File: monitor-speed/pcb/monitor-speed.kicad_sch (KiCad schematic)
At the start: 1 part

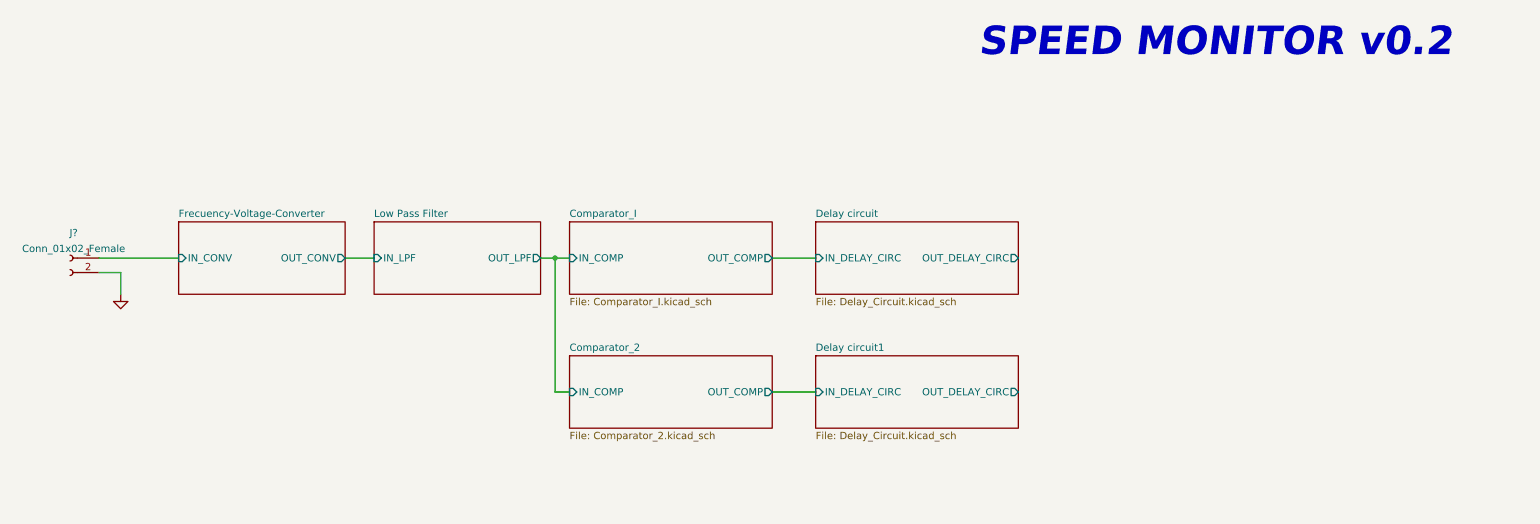
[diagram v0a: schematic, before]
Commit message: Monitor-Speed: Add pcb edge
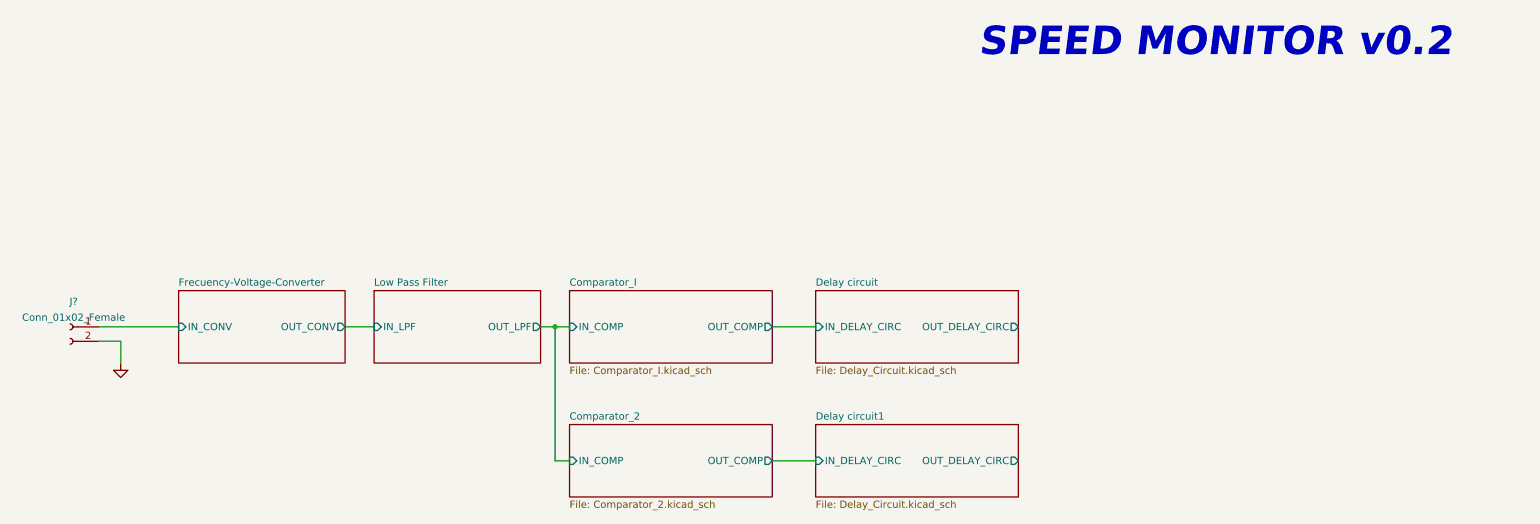
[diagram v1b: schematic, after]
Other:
- moved on the sheet: J?
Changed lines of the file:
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@@
 (kicad_sch (version 20211123) (generator eeschema)
   (paper "A4")
-  (junction (at 114.935 65.405) (diameter 0) (color 0 0 0 0)
+  (junction (at 114.935 77.47) (diameter 0) (color 0 0 0 0)
   )
-  (wire (pts (xy 78.105 65.405) (xy 83.185 65.405))
+  (wire (pts (xy 78.105 77.47) (xy 83.185 77.47))
     (stroke (width 0) (type default) (color 0 0 0 0))
   )
-  (wire (pts (xy 114.935 65.405) (xy 117.475 65.405))
+  (wire (pts (xy 114.935 77.47) (xy 117.475 77.47))
     (stroke (width 0) (type default) (color 0 0 0 0))
   )
-  (wire (pts (xy 153.035 88.9) (xy 160.655 88.9))
+  (wire (pts (xy 153.035 100.965) (xy 160.655 100.965))
     (stroke (width 0) (type default) (color 0 0 0 0))
   )
-  (wire (pts (xy 34.925 65.405) (xy 48.895 65.405))
+  (wire (pts (xy 34.925 77.47) (xy 48.895 77.47))
     (stroke (width 0) (type default) (color 0 0 0 0))
   )
-  (wire (pts (xy 38.735 67.945) (xy 38.735 71.755))
+  (wire (pts (xy 38.735 80.01) (xy 38.735 83.82))
     (stroke (width 0) (type default) (color 0 0 0 0))
   )
-  (wire (pts (xy 114.935 65.405) (xy 114.935 88.9))
+  (wire (pts (xy 114.935 77.47) (xy 114.935 100.965))
     (stroke (width 0) (type default) (color 0 0 0 0))
   )
-  (wire (pts (xy 153.035 65.405) (xy 160.655 65.405))
+  (wire (pts (xy 153.035 77.47) (xy 160.655 77.47))
     (stroke (width 0) (type default) (color 0 0 0 0))
   )
-  (wire (pts (xy 114.935 88.9) (xy 117.475 88.9))
+  (wire (pts (xy 114.935 100.965) (xy 117.475 100.965))
     (stroke (width 0) (type default) (color 0 0 0 0))
   )
-  (wire (pts (xy 34.925 67.945) (xy 38.735 67.945))
+  (wire (pts (xy 34.925 80.01) (xy 38.735 80.01))
     (stroke (width 0) (type default) (color 0 0 0 0))
   )
-  (wire (pts (xy 112.395 65.405) (xy 114.935 65.405))
+  (wire (pts (xy 112.395 77.47) (xy 114.935 77.47))
     (stroke (width 0) (type default) (color 0 0 0 0))
   )
@@
     (effects (font (size 5 5) (thickness 1) bold italic) (justify left bottom))
   )
-  (symbol (lib_id "power:GND") (at 38.735 71.755 0) (unit 1)
+  (symbol (lib_id "power:GND") (at 38.735 83.82 0) (unit 1)
     (in_bom yes) (on_board yes) (fields_autoplaced)
-    (property "Reference" "#PWR?" (id 0) (at 38.735 78.105 0)
+    (property "Reference" "#PWR?" (id 0) (at 38.735 90.17 0)
       (effects (font (size 1.27 1.27)) hide)
     )
-    (property "Value" "GND" (id 1) (at 38.735 76.3175 0)
+    (property "Value" "GND" (id 1) (at 38.735 88.3825 0)
       (effects (font (size 1.27 1.27)) hide)
     )
-    (property "Footprint" "" (id 2) (at 38.735 71.755 0)
+    (property "Footprint" "" (id 2) (at 38.735 83.82 0)
       (effects (font (size 1.27 1.27)) hide)
     )
-    (property "Datasheet" "" (id 3) (at 38.735 71.755 0)
+    (property "Datasheet" "" (id 3) (at 38.735 83.82 0)
       (effects (font (size 1.27 1.27)) hide)
     )
     (pin "1")
   )
-  (symbol (lib_id "Connector:Conn_01x02_Female") (at 29.845 65.405 0) (mirror y) (unit 1)
+  (symbol (lib_id "Connector:Conn_01x02_Female") (at 29.845 77.47 0) (mirror y) (unit 1)
     (in_bom yes) (on_board yes) (fields_autoplaced)
-    (property "Reference" "J?" (id 0) (at 30.48 60.9813 0))
-    (property "Value" "Conn_01x02_Female" (id 1) (at 30.48 63.7564 0))
-    (property "Footprint" "" (id 2) (at 29.845 65.405 0)
+    (property "Reference" "J?" (id 0) (at 30.48 73.0463 0))
+    (property "Value" "Conn_01x02_Female" (id 1) (at 30.48 75.8214 0))
+    (property "Footprint" "" (id 2) (at 29.845 77.47 0)
       (effects (font (size 1.27 1.27)) hide)
     )
-    (property "Datasheet" "~" (id 3) (at 29.845 65.405 0)
+    (property "Datasheet" "~" (id 3) (at 29.845 77.47 0)
       (effects (font (size 1.27 1.27)) hide)
     )
@@
     (pin "2")
   )
-  (sheet (at 48.895 59.055) (size 29.21 12.7) (fields_autoplaced)
+  (sheet (at 48.895 71.12) (size 29.21 12.7) (fields_autoplaced)
     (stroke (width 0.1524) (type solid) (color 0 0 0 0))
     (fill (color 0 0 0 0.0000))
-    (property "Sheet name" "Frecuency-Voltage-Converter" (id 0) (at 48.895 58.3434 0)
+    (property "Sheet name" "Frecuency-Voltage-Converter" (id 0) (at 48.895 70.4084 0)
       (effects (font (size 1.27 1.27)) (justify left bottom))
     )
-    (property "Sheet file" "Frecuency_voltage_converter.kicad_sch" (id 1) (at 48.895 72.3396 0)
+    (property "Sheet file" "Frecuency_voltage_converter.kicad_sch" (id 1) (at 48.895 84.4046 0)
       (effects (font (size 1.27 1.27)) (justify left top) hide)
     )
-    (pin "IN_CONV" input (at 48.895 65.405 180)
+    (pin "IN_CONV" input (at 48.895 77.47 180)
       (effects (font (size 1.27 1.27)) (justify left))
     )
-    (pin "OUT_CONV" output (at 78.105 65.405 0)
+    (pin "OUT_CONV" output (at 78.105 77.47 0)
       (effects (font (size 1.27 1.27)) (justify right))
     )
   )
-  (sheet (at 160.655 82.55) (size 35.56 12.7) (fields_autoplaced)
+  (sheet (at 160.655 94.615) (size 35.56 12.7) (fields_autoplaced)
     (stroke (width 0.1524) (type solid) (color 0 0 0 0))
     (fill (color 0 0 0 0.0000))
-    (property "Sheet name" "Delay circuit1" (id 0) (at 160.655 81.8384 0)
+    (property "Sheet name" "Delay circuit1" (id 0) (at 160.655 93.9034 0)
       (effects (font (size 1.27 1.27)) (justify left bottom))
     )
-    (property "Sheet file" "Delay_Circuit.kicad_sch" (id 1) (at 160.655 95.8346 0)
+    (property "Sheet file" "Delay_Circuit.kicad_sch" (id 1) (at 160.655 107.8996 0)
       (effects (font (size 1.27 1.27)) (justify left top))
     )
-    (pin "IN_DELAY_CIRC" input (at 160.655 88.9 180)
+    (pin "IN_DELAY_CIRC" input (at 160.655 100.965 180)
       (effects (font (size 1.27 1.27)) (justify left))
     )
-    (pin "OUT_DELAY_CIRC" output (at 196.215 88.9 0)
+    (pin "OUT_DELAY_CIRC" output (at 196.215 100.965 0)
       (effects (font (size 1.27 1.27)) (justify right))
     )
   )
-  (sheet (at 117.475 82.55) (size 35.56 12.7) (fields_autoplaced)
+  (sheet (at 117.475 94.615) (size 35.56 12.7) (fields_autoplaced)
     (stroke (width 0.1524) (type solid) (color 0 0 0 0))
     (fill (color 0 0 0 0.0000))
-    (property "Sheet name" "Comparator_2" (id 0) (at 117.475 81.8384 0)
+    (property "Sheet name" "Comparator_2" (id 0) (at 117.475 93.9034 0)
       (effects (font (size 1.27 1.27)) (justify left bottom))
     )
-    (property "Sheet file" "Comparator_2.kicad_sch" (id 1) (at 117.475 95.8346 0)
+    (property "Sheet file" "Comparator_2.kicad_sch" (id 1) (at 117.475 107.8996 0)
       (effects (font (size 1.27 1.27)) (justify left top))
     )
-    (pin "IN_COMP" input (at 117.475 88.9 180)
+    (pin "IN_COMP" input (at 117.475 100.965 180)
       (effects (font (size 1.27 1.27)) (justify left))
     )
-    (pin "OUT_COMP" output (at 153.035 88.9 0)
+    (pin "OUT_COMP" output (at 153.035 100.965 0)
       (effects (font (size 1.27 1.27)) (justify right))
     )
   )
-  (sheet (at 160.655 59.055) (size 35.56 12.7) (fields_autoplaced)
+  (sheet (at 160.655 71.12) (size 35.56 12.7) (fields_autoplaced)
     (stroke (width 0.1524) (type solid) (color 0 0 0 0))
     (fill (color 0 0 0 0.0000))
-    (property "Sheet name" "Delay circuit" (id 0) (at 160.655 58.3434 0)
+    (property "Sheet name" "Delay circuit" (id 0) (at 160.655 70.4084 0)
       (effects (font (size 1.27 1.27)) (justify left bottom))
     )
-    (property "Sheet file" "Delay_Circuit.kicad_sch" (id 1) (at 160.655 72.3396 0)
+    (property "Sheet file" "Delay_Circuit.kicad_sch" (id 1) (at 160.655 84.4046 0)
       (effects (font (size 1.27 1.27)) (justify left top))
     )
-    (pin "IN_DELAY_CIRC" input (at 160.655 65.405 180)
+    (pin "IN_DELAY_CIRC" input (at 160.655 77.47 180)
       (effects (font (size 1.27 1.27)) (justify left))
     )
-    (pin "OUT_DELAY_CIRC" output (at 196.215 65.405 0)
+    (pin "OUT_DELAY_CIRC" output (at 196.215 77.47 0)
       (effects (font (size 1.27 1.27)) (justify right))
     )
   )
-  (sheet (at 117.475 59.055) (size 35.56 12.7) (fields_autoplaced)
+  (sheet (at 117.475 71.12) (size 35.56 12.7) (fields_autoplaced)
     (stroke (width 0.1524) (type solid) (color 0 0 0 0))
     (fill (color 0 0 0 0.0000))
-    (property "Sheet name" "Comparator_I" (id 0) (at 117.475 58.3434 0)
+    (property "Sheet name" "Comparator_I" (id 0) (at 117.475 70.4084 0)
       (effects (font (size 1.27 1.27)) (justify left bottom))
     )
-    (property "Sheet file" "Comparator_I.kicad_sch" (id 1) (at 117.475 72.3396 0)
+    (property "Sheet file" "Comparator_I.kicad_sch" (id 1) (at 117.475 84.4046 0)
       (effects (font (size 1.27 1.27)) (justify left top))
     )
-    (pin "IN_COMP" input (at 117.475 65.405 180)
+    (pin "IN_COMP" input (at 117.475 77.47 180)
       (effects (font (size 1.27 1.27)) (justify left))
     )
-    (pin "OUT_COMP" output (at 153.035 65.405 0)
+    (pin "OUT_COMP" output (at 153.035 77.47 0)
       (effects (font (size 1.27 1.27)) (justify right))
     )
   )
-  (sheet (at 83.185 59.055) (size 29.21 12.7) (fields_autoplaced)
+  (sheet (at 83.185 71.12) (size 29.21 12.7) (fields_autoplaced)
     (stroke (width 0.1524) (type solid) (color 0 0 0 0))
     (fill (color 0 0 0 0.0000))
-    (property "Sheet name" "Low Pass Filter" (id 0) (at 83.185 58.3434 0)
+    (property "Sheet name" "Low Pass Filter" (id 0) (at 83.185 70.4084 0)
       (effects (font (size 1.27 1.27)) (justify left bottom))
     )
-    (property "Sheet file" "Low_pass_filter.kicad_sch" (id 1) (at 83.185 72.3396 0)
+    (property "Sheet file" "Low_pass_filter.kicad_sch" (id 1) (at 83.185 84.4046 0)
       (effects (font (size 1.27 1.27)) (justify left top) hide)
     )
-    (pin "OUT_LPF" output (at 112.395 65.405 0)
+    (pin "OUT_LPF" output (at 112.395 77.47 0)
       (effects (font (size 1.27 1.27)) (justify right))
     )
-    (pin "IN_LPF" input (at 83.185 65.405 180)
+    (pin "IN_LPF" input (at 83.185 77.47 180)
       (effects (font (size 1.27 1.27)) (justify left))
     )
